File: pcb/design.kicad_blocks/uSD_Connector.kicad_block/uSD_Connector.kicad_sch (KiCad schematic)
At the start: 10 parts, among them J3 Micro_SD_Card

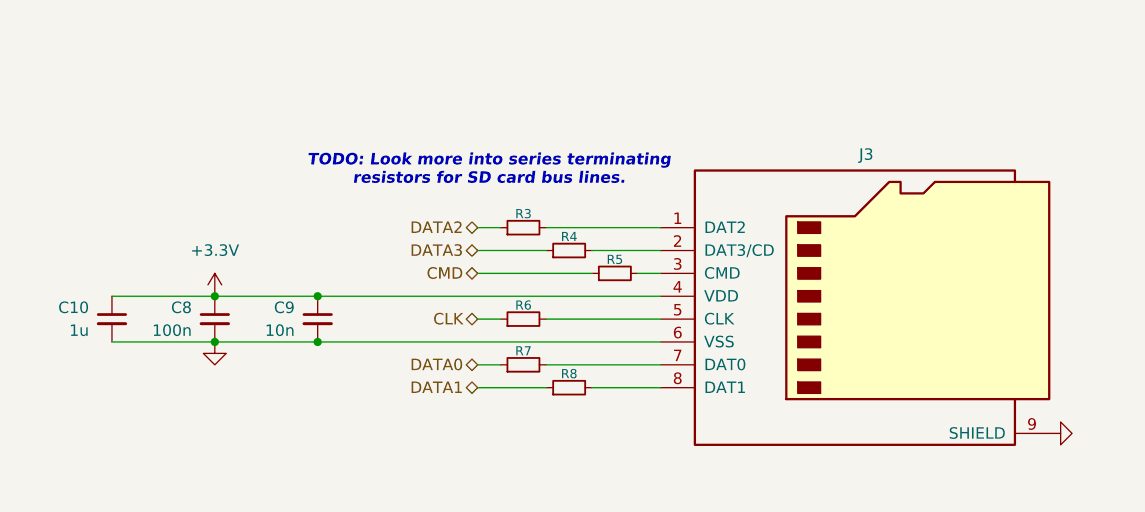
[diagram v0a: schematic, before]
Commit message: Trying out design blocks instead of hierarchal sheets.
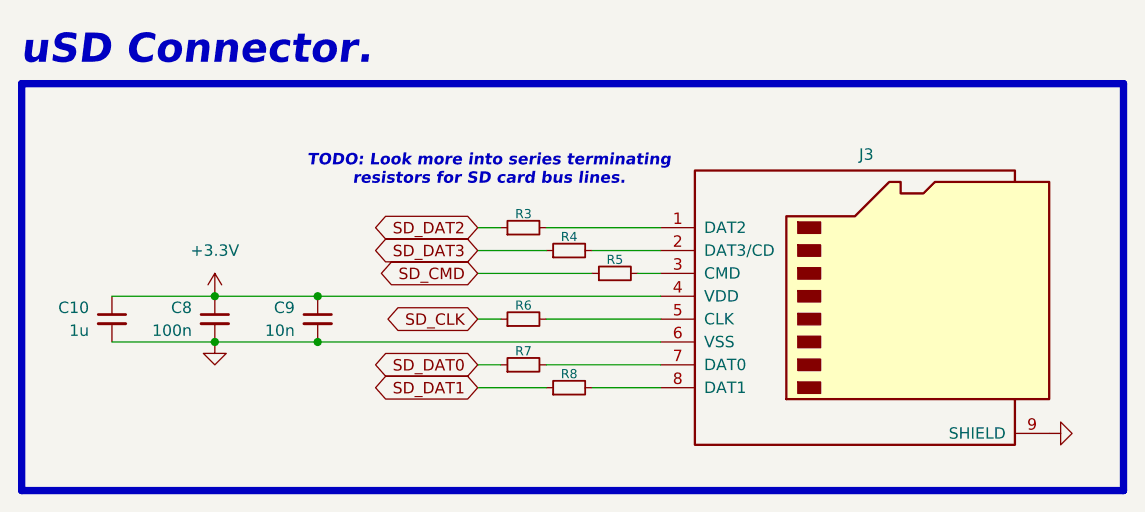
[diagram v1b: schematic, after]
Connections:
- net CLK renamed SD_CLK
- net CMD renamed SD_CMD
- net DATA0 renamed SD_DAT0
- net DATA1 renamed SD_DAT1
- net DATA2 renamed SD_DAT2
- net DATA3 renamed SD_DAT3
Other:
- note added: "uSD Connector."
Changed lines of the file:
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@@
 	(generator_version "9.0")
 	(paper "A4")
+	(rectangle
+		(start 75.057 76.708)
+		(end 197.485 121.92)
+		(stroke
+			(width 0.8128)
+			(type solid)
+			(color 255 0 0 1)
+		)
+		(fill
+			(type none)
+		)
+	)
 	(text "TODO: Look more into series terminating\nresistors for SD card bus lines."
 		(exclude_from_sim no)
@@
 		)
 	)
+	(text "uSD Connector."
+		(exclude_from_sim no)
+		(at 74.93 74.93 0)
+		(effects
+			(font
+				(size 3.2512 3.2512)
+				(thickness 0.6502)
+				(bold yes)
+				(italic yes)
+				(color 255 0 0 1)
+			)
+			(justify left bottom)
+		)
+	)
 	(junction
 		(at 96.52 100.33)
@@
 		)
 	)
-	(hierarchical_label "CLK"
+	(global_label "SD_CMD"
+		(shape bidirectional)
+		(at 125.73 97.79 180)
+		(fields_autoplaced yes)
+		(effects
+			(font
+				(size 1.27 1.27)
+			)
+			(justify right)
+		)
+		(property "Intersheetrefs" "${INTERSHEET_REFS}"
+			(at 114.195 97.79 0)
+			(effects
+				(font
+					(size 1.27 1.27)
+				)
+				(justify right)
+				(hide yes)
+			)
+		)
+	)
+	(global_label "SD_DAT1"
+		(shape bidirectional)
+		(at 125.73 110.49 180)
+		(fields_autoplaced yes)
+		(effects
+			(font
+				(size 1.27 1.27)
+			)
+			(justify right)
+		)
+		(property "Intersheetrefs" "${INTERSHEET_REFS}"
+			(at 113.6507 110.49 0)
+			(effects
+				(font
+					(size 1.27 1.27)
+				)
+				(justify right)
+				(hide yes)
+			)
+		)
+	)
+	(global_label "SD_DAT2"
+		(shape bidirectional)
+		(at 125.73 92.71 180)
+		(fields_autoplaced yes)
+		(effects
+			(font
+				(size 1.27 1.27)
+			)
+			(justify right)
+		)
+		(property "Intersheetrefs" "${INTERSHEET_REFS}"
+			(at 113.6507 92.71 0)
+			(effects
+				(font
+					(size 1.27 1.27)
+				)
+				(justify right)
+				(hide yes)
+			)
+		)
+	)
+	(global_label "SD_DAT0"
+		(shape bidirectional)
+		(at 125.73 107.95 180)
+		(fields_autoplaced yes)
+		(effects
+			(font
+				(size 1.27 1.27)
+			)
+			(justify right)
+		)
+		(property "Intersheetrefs" "${INTERSHEET_REFS}"
+			(at 113.6507 107.95 0)
+			(effects
+				(font
+					(size 1.27 1.27)
+				)
+				(justify right)
+				(hide yes)
+			)
+		)
+	)
+	(global_label "SD_CLK"
 		(shape bidirectional)
 		(at 125.73 102.87 180)
-		(effects
-			(font
-				(size 1.27 1.27)
-			)
-			(justify right)
-		)
-	)
-	(hierarchical_label "DATA3"
+		(fields_autoplaced yes)
+		(effects
+			(font
+				(size 1.27 1.27)
+			)
+			(justify right)
+		)
+		(property "Intersheetrefs" "${INTERSHEET_REFS}"
+			(at 114.6183 102.87 0)
+			(effects
+				(font
+					(size 1.27 1.27)
+				)
+				(justify right)
+				(hide yes)
+			)
+		)
+	)
+	(global_label "SD_DAT3"
 		(shape bidirectional)
 		(at 125.73 95.25 180)
-		(effects
-			(font
-				(size 1.27 1.27)
-			)
-			(justify right)
-		)
-	)
-	(hierarchical_label "DATA0"
-		(shape bidirectional)
-		(at 125.73 107.95 180)
-		(effects
-			(font
-				(size 1.27 1.27)
-			)
-			(justify right)
-		)
-	)
-	(hierarchical_label "CMD"
-		(shape bidirectional)
-		(at 125.73 97.79 180)
-		(effects
-			(font
-				(size 1.27 1.27)
-			)
-			(justify right)
-		)
-	)
-	(hierarchical_label "DATA1"
-		(shape bidirectional)
-		(at 125.73 110.49 180)
-		(effects
-			(font
-				(size 1.27 1.27)
-			)
-			(justify right)
-		)
-	)
-	(hierarchical_label "DATA2"
-		(shape bidirectional)
-		(at 125.73 92.71 180)
-		(effects
-			(font
-				(size 1.27 1.27)
-			)
-			(justify right)
-		)
-	)
+		(fields_autoplaced yes)
+		(effects
+			(font
+				(size 1.27 1.27)
+			)
+			(justify right)
+		)
+		(property "Intersheetrefs" "${INTERSHEET_REFS}"
+			(at 113.6507 95.25 0)
+			(effects
+				(font
+					(size 1.27 1.27)
+				)
+				(justify right)
+				(hide yes)
+			)
+		)
+	)

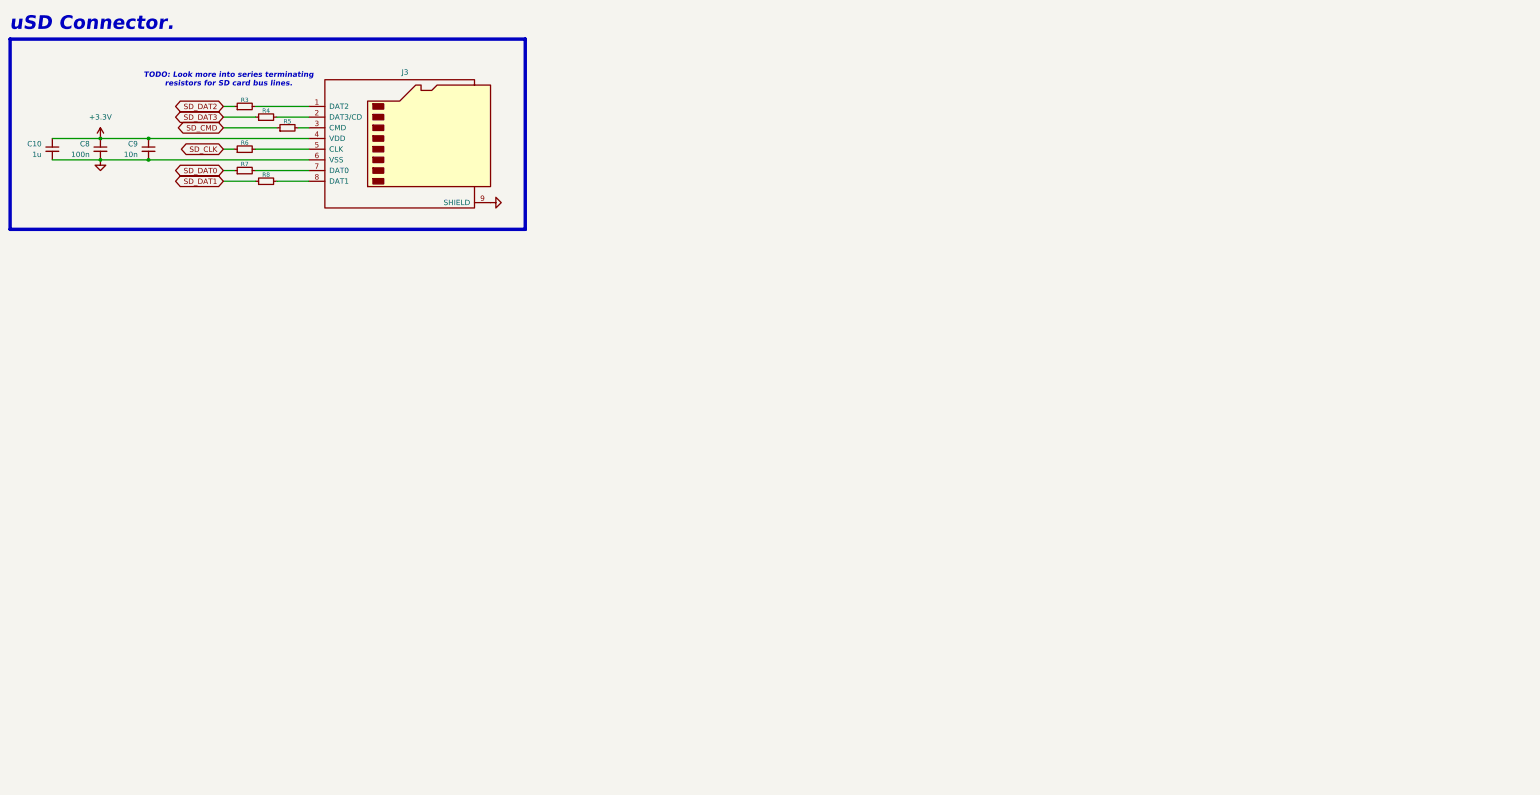
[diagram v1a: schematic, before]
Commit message: Added some missing pins.
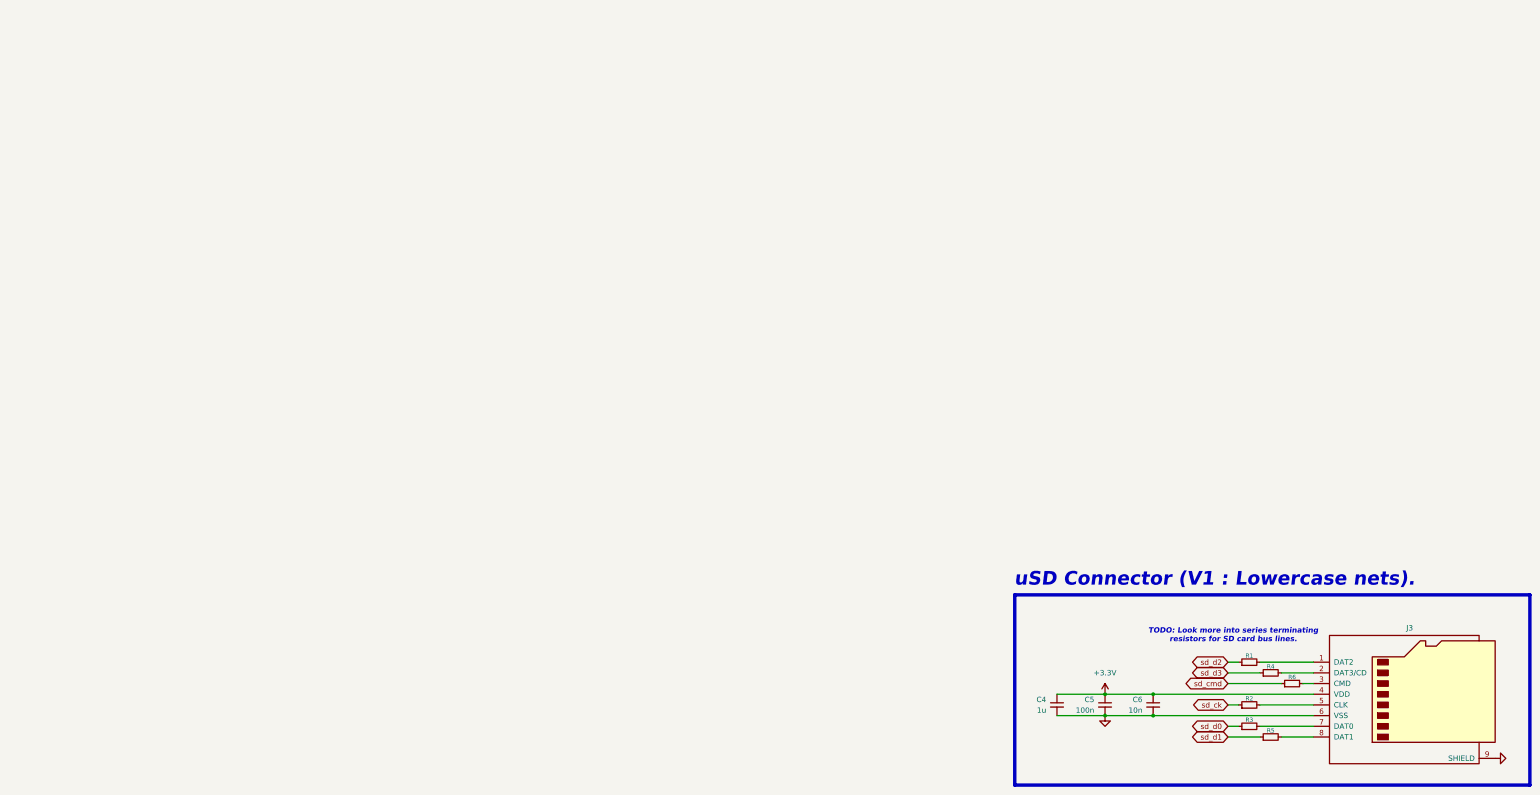
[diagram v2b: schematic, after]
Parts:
- renumbered C10 to C4, C8 to C5, C9 to C6, R3 to R1, R6 to R2, R7 to R3, R8 to R5, R5 to R6
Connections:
- net SD_CLK renamed sd_ck
- net SD_CMD renamed sd_cmd
- net SD_DAT0 renamed sd_d0
- net SD_DAT1 renamed sd_d1
- net SD_DAT2 renamed sd_d2
- net SD_DAT3 renamed sd_d3
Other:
- note added: "uSD Connector (V1 : Lowercase nets)."
- note removed: "uSD Connector."
- moved on the sheet: C4, C5, C6, J3, R1, R2, R3, R4, R5, R6

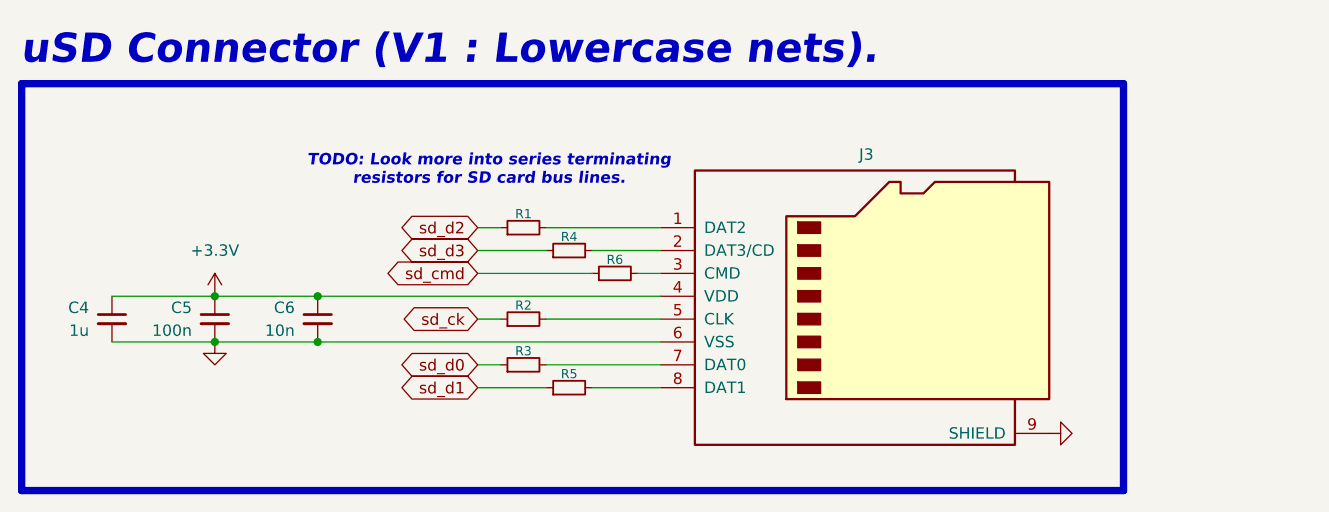
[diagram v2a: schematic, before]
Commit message: More verbose net-names for uSD connector.
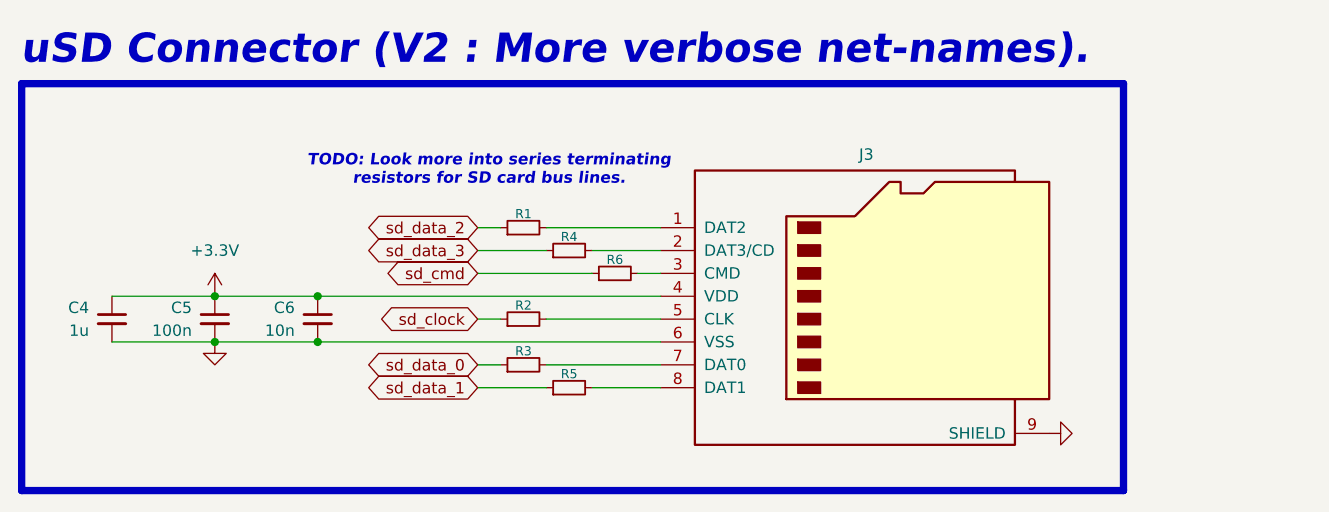
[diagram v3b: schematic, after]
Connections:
- net sd_ck renamed sd_clock
- net sd_d0 renamed sd_data_0
- net sd_d1 renamed sd_data_1
- net sd_d2 renamed sd_data_2
- net sd_d3 renamed sd_data_3
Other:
- note added: "uSD Connector (V2 : More verbose net-names)."
- note removed: "uSD Connector (V1 : Lowercase nets)."
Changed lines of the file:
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@@
 		)
 	)
-	(text "uSD Connector (V1 : Lowercase nets)."
+	(text "uSD Connector (V2 : More verbose net-names)."
 		(exclude_from_sim no)
 		(at 313.69 207.01 0)
@@
 		)
 	)
-	(global_label "sd_d1"
+	(global_label "sd_data_1"
 		(shape bidirectional)
 		(at 364.49 242.57 180)
@@
 		)
 		(property "Intersheetrefs" "${INTERSHEET_REFS}"
-			(at 354.8903 242.57 0)
-			(effects
-				(font
-					(size 1.27 1.27)
-				)
-				(justify right)
-				(hide yes)
-			)
-		)
-	)
-	(global_label "sd_d2"
+			(at 350.899 242.57 0)
+			(effects
+				(font
+					(size 1.27 1.27)
+				)
+				(justify right)
+				(hide yes)
+			)
+		)
+	)
+	(global_label "sd_data_2"
 		(shape bidirectional)
 		(at 364.49 224.79 180)
@@
 		)
 		(property "Intersheetrefs" "${INTERSHEET_REFS}"
-			(at 354.8903 224.79 0)
-			(effects
-				(font
-					(size 1.27 1.27)
-				)
-				(justify right)
-				(hide yes)
-			)
-		)
-	)
-	(global_label "sd_d0"
+			(at 350.899 224.79 0)
+			(effects
+				(font
+					(size 1.27 1.27)
+				)
+				(justify right)
+				(hide yes)
+			)
+		)
+	)
+	(global_label "sd_data_0"
 		(shape bidirectional)
 		(at 364.49 240.03 180)
@@
 		)
 		(property "Intersheetrefs" "${INTERSHEET_REFS}"
-			(at 354.8903 240.03 0)
-			(effects
-				(font
-					(size 1.27 1.27)
-				)
-				(justify right)
-				(hide yes)
-			)
-		)
-	)
-	(global_label "sd_ck"
+			(at 350.899 240.03 0)
+			(effects
+				(font
+					(size 1.27 1.27)
+				)
+				(justify right)
+				(hide yes)
+			)
+		)
+	)
+	(global_label "sd_clock"
 		(shape bidirectional)
 		(at 364.49 234.95 180)
@@
 		)
 		(property "Intersheetrefs" "${INTERSHEET_REFS}"
-			(at 355.1321 234.95 0)
-			(effects
-				(font
-					(size 1.27 1.27)
-				)
-				(justify right)
-				(hide yes)
-			)
-		)
-	)
-	(global_label "sd_d3"
+			(at 352.2293 234.95 0)
+			(effects
+				(font
+					(size 1.27 1.27)
+				)
+				(justify right)
+				(hide yes)
+			)
+		)
+	)
+	(global_label "sd_data_3"
 		(shape bidirectional)
 		(at 364.49 227.33 180)
@@
 		)
 		(property "Intersheetrefs" "${INTERSHEET_REFS}"
-			(at 354.8903 227.33 0)
-			(effects
-				(font
+			(at 350.899 227.33 0)
+			(effects
+				(font

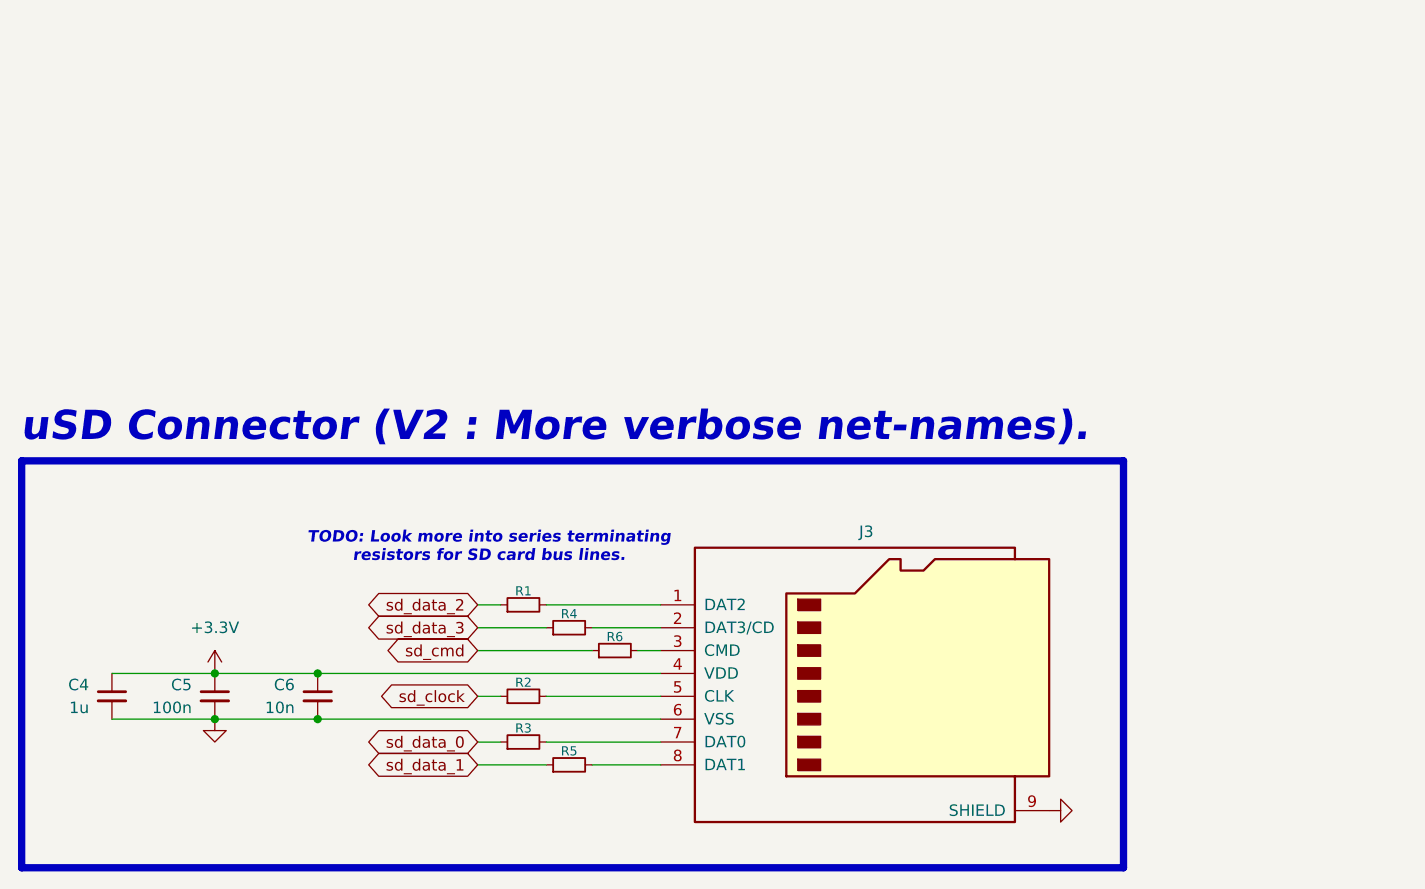
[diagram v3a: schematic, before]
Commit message: Routed uSD connector.
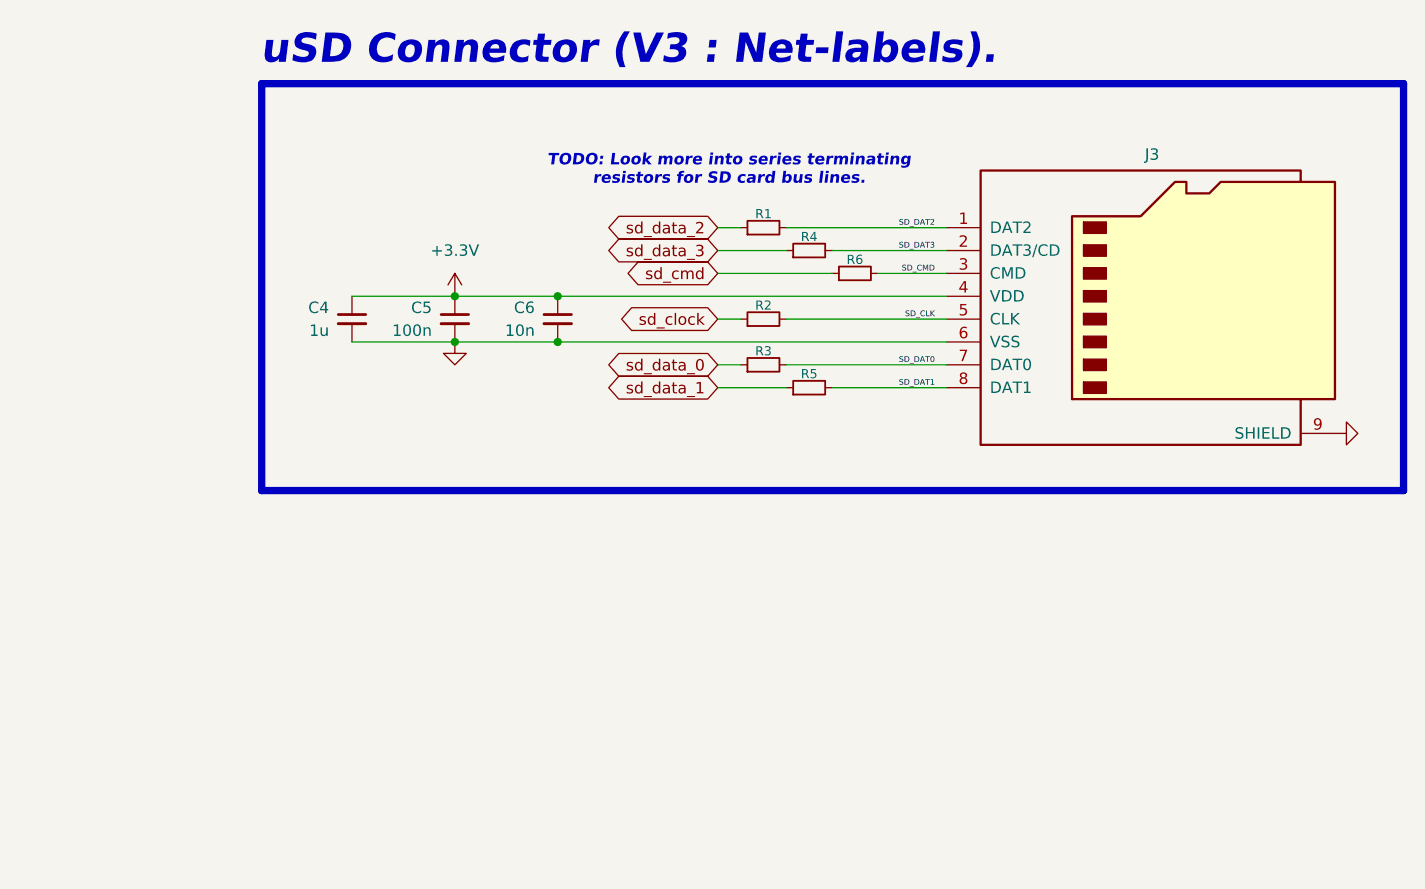
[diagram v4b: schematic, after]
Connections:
- net SD_DAT2: now reaches J3.1 (DAT2), R1.2
- net SD_CLK: now reaches J3.5 (CLK), R2.2
- net SD_DAT3: now reaches J3.2 (DAT3/CD), R4.2
- net SD_DAT0: now reaches J3.7 (DAT0), R3.2
- net SD_CMD: now reaches J3.3 (CMD), R6.2
- net SD_DAT1: now reaches J3.8 (DAT1), R5.2
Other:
- note added: "uSD Connector (V3 : Net-labels)."
- note removed: "uSD Connector (V2 : More verbose net-names)."
- moved on the sheet: C4, C5, C6, J3, R1, R2, R3, R4, R5, R6
